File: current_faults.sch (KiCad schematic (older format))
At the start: 7 parts, among them U4 LMV393, U5 LMV393, U6 74LS32

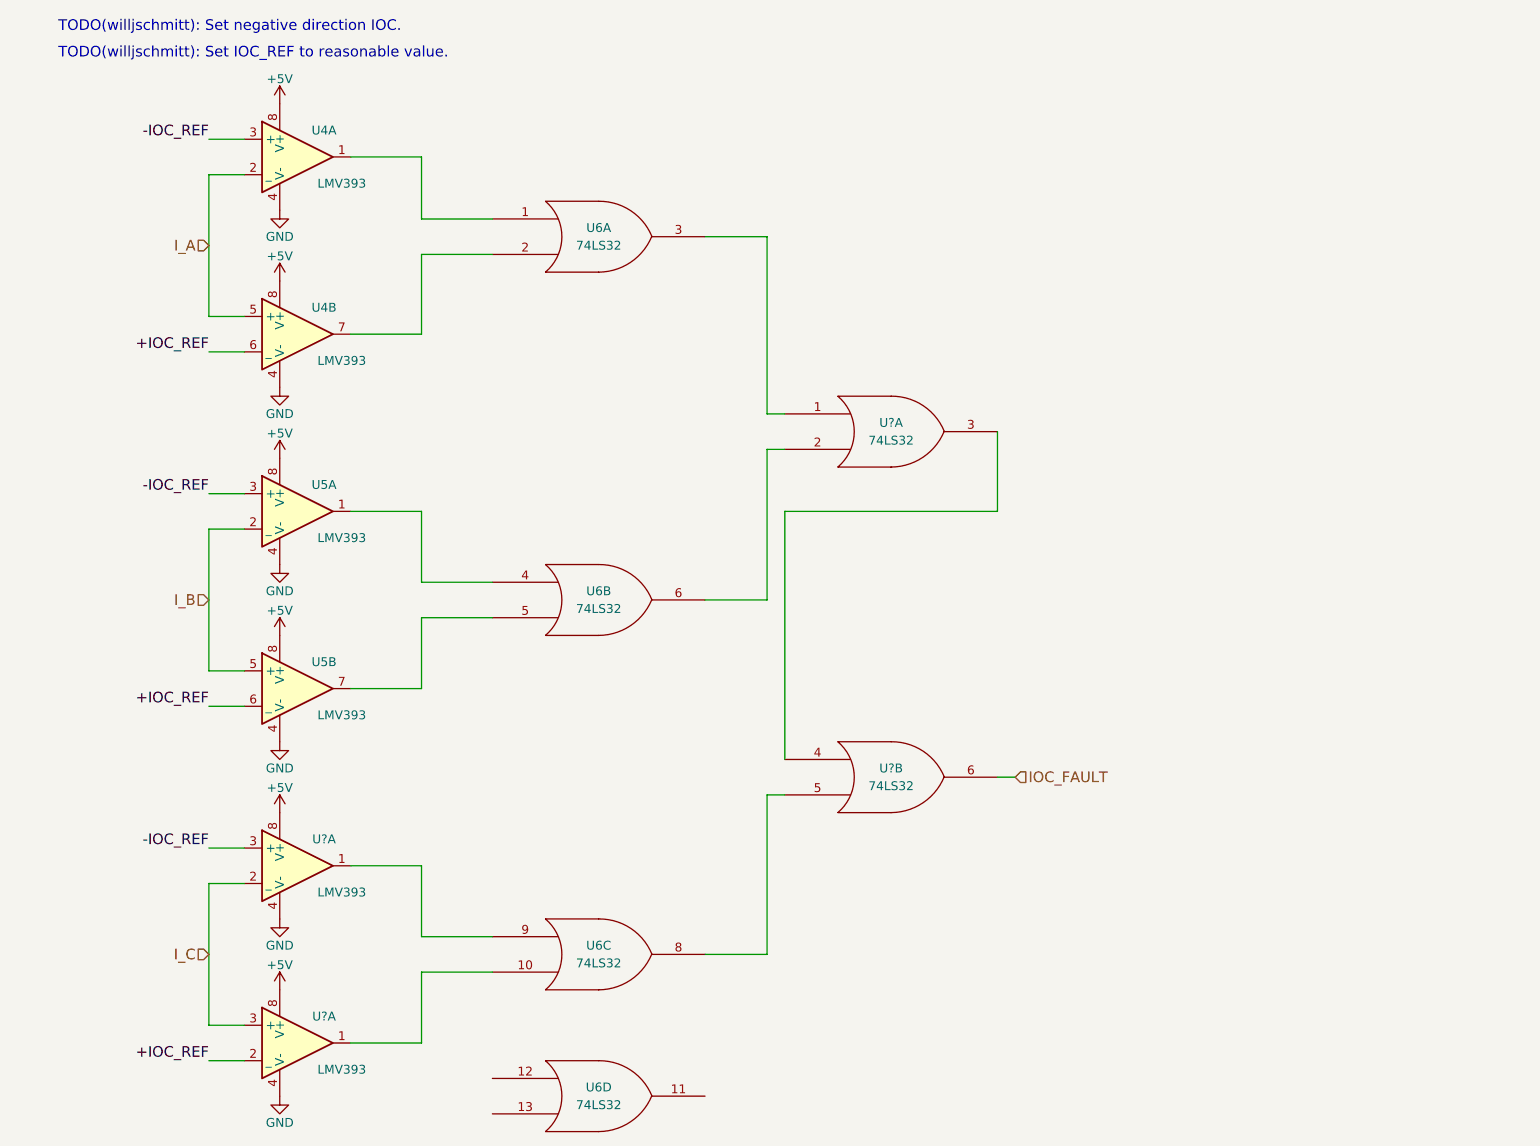
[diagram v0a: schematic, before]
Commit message: Adds IOC reference points.
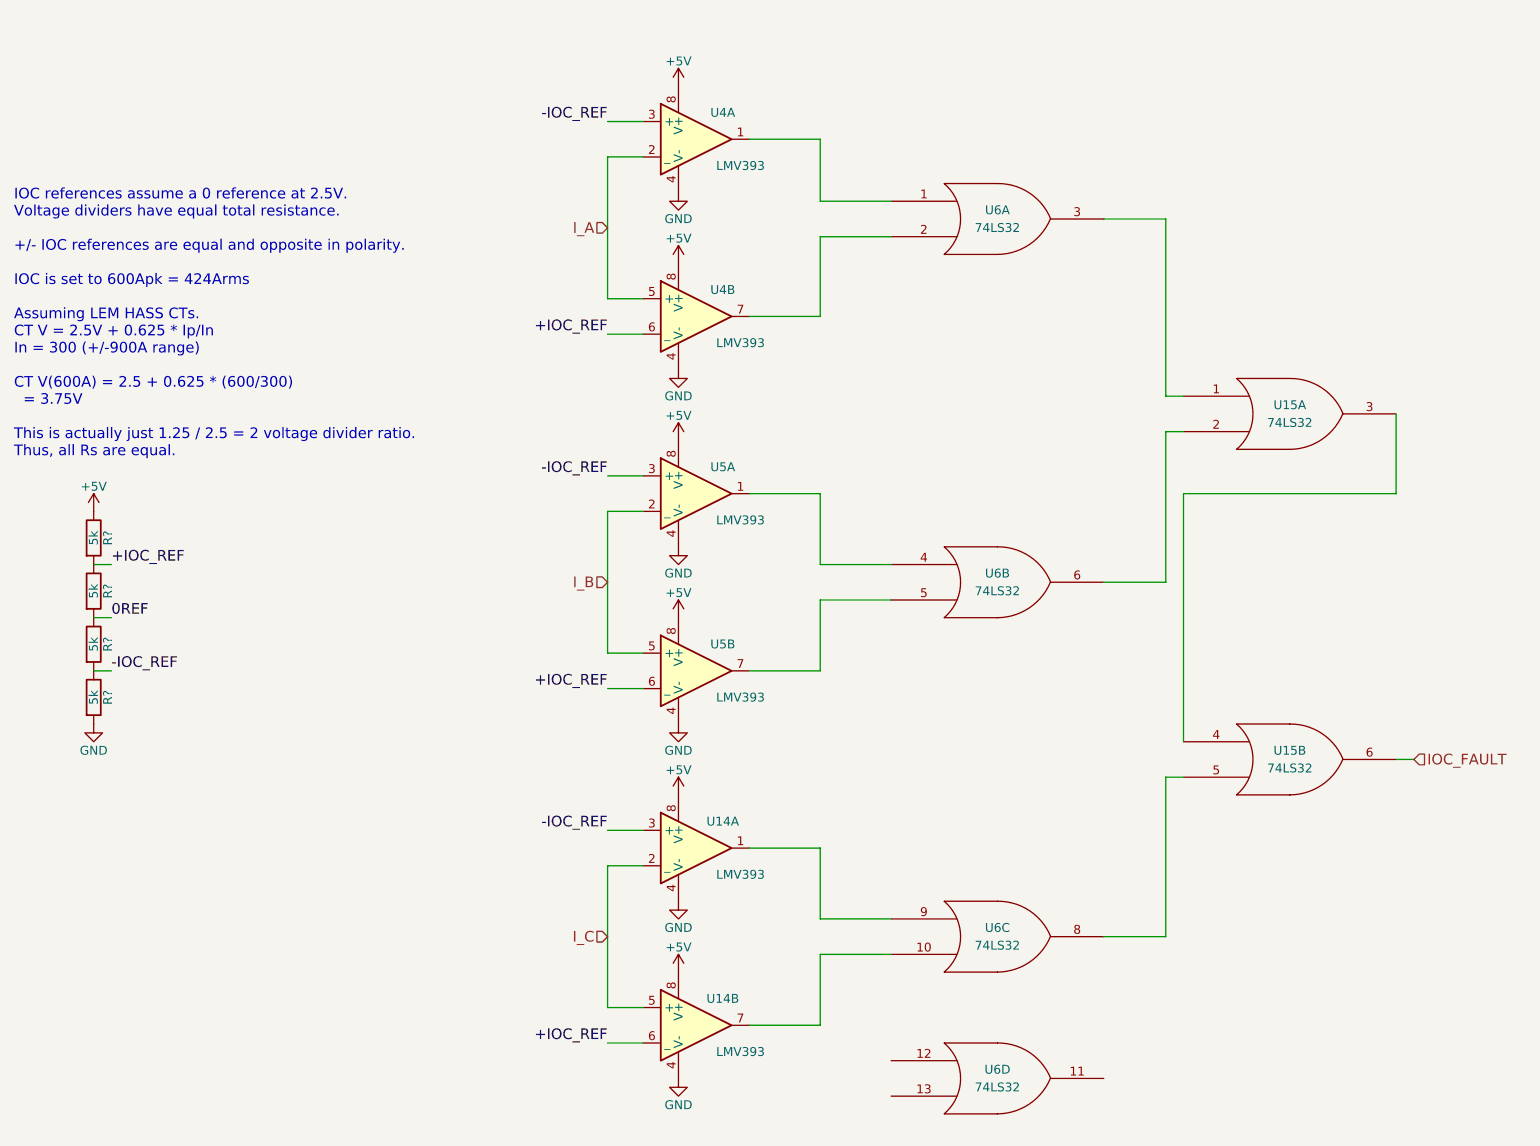
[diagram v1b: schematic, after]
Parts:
- added R? (x4): 5k, symbol R
- gave numbers to parts that had none: 2
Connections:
- net +5V: now also R?.1
- net +IOC_REF: now also U14.6 (_), R?.1, R?.2; no longer U14.2 (_)
- net -IOC_REF: now also R?.1, R?.2
- net GND: now also R?.2
- net I_C: now also U14.5 (+); no longer U14.3 (+)
- net at U6.10: now also U14.7; no longer U14.1
- new net 0REF: R?.1, R?.2
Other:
- note added: "IOC references assume a 0 reference at 2.5V.\nVoltage dividers have equal total resistance.\n\n+/- IOC references are equal and opposite in polarity.\n\nIOC is set to 600Apk = 424Arms\n\nAssuming LEM HASS CTs.\nCT V = 2.5V + 0.625 * Ip/In\nIn = 300 (+/-900A range)\n\nCT V(600A) = 2.5 + 0.625 * (600/300)\n = 3.75V\n\nThis is actually just 1.25 / 2.5 = 2 voltage divider ratio.\nThus, all Rs are equ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"
- note removed: "TODO(willjschmitt): Set IOC_REF to reasonable value."
- note removed: "TODO(willjschmitt): Set negative direction IOC."
- moved on the sheet: U14A, U15A, U15B, U4A, U4B, U5A, U5B, U6A, U6B, U6C, U6D
